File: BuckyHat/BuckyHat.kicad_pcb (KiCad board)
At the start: 6 copper layers, 97.2 x 53.7 mm, 95 parts, among them IC1 LM61495Q4RPHRQ1, IC2 LM61495Q4RPHRQ1, IC3 LM61495Q4RPHRQ1, IC4 LM61495Q4RPHRQ1, J1 XT30AW-M, J2 XT30UPB-F, J3 XT30AW-M, J4 XT30UPB-F, J5 XT30AW-M, J6 XT30UPB-F, J7 XT30AW-M, J8 XT30UPB-F

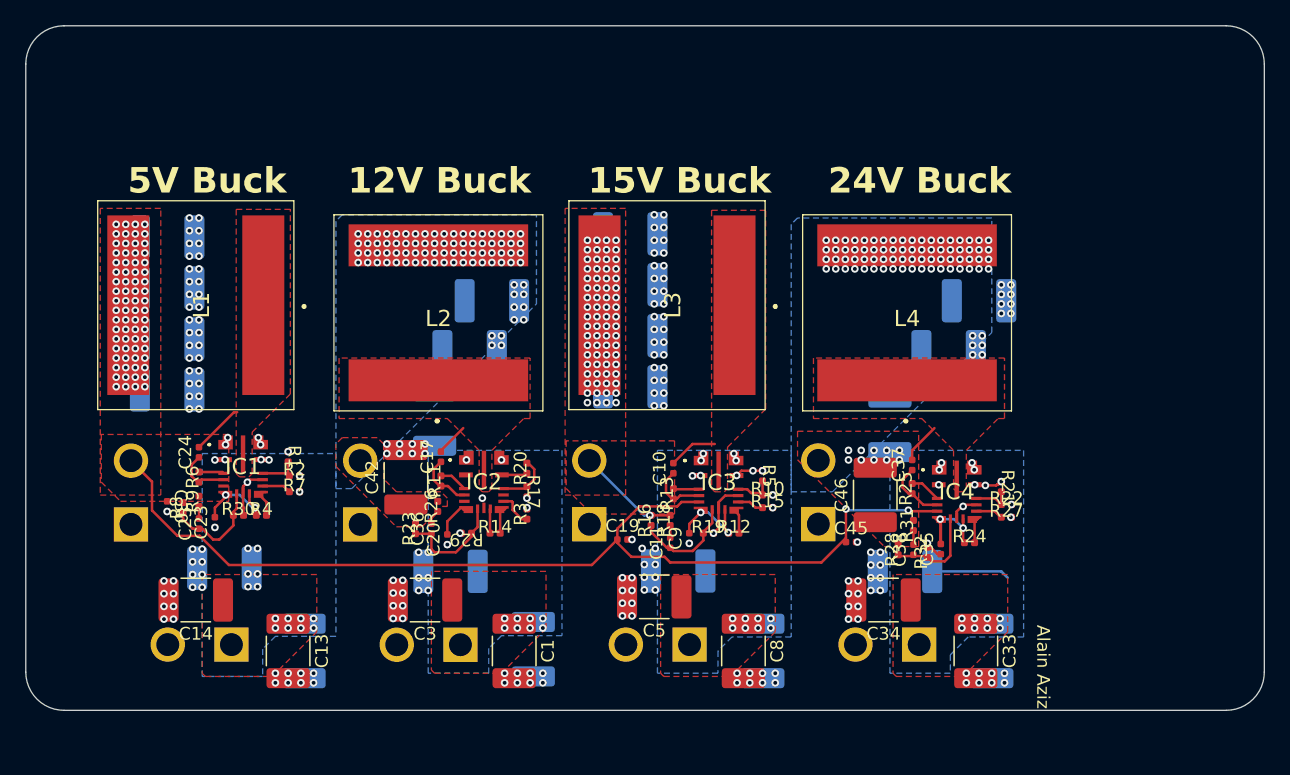
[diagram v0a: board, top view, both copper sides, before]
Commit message: no DRC errors
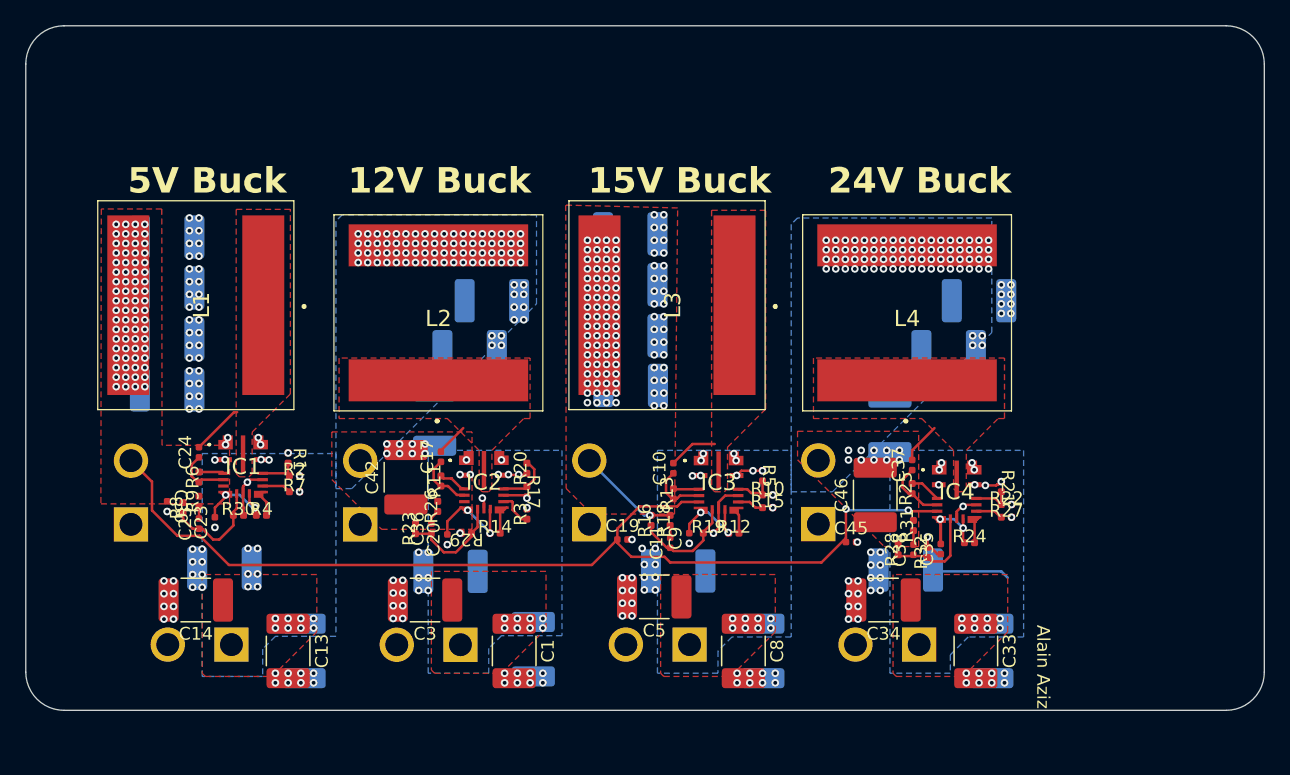
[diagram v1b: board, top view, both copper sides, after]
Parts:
- moved C32 0.13 mm to (217.0, 90.4)
- moved C18 0.11 mm to (195.4, 75.9)
- moved R1 0.10 mm to (168.5, 81.6)
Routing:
- net GND: track 11.9 -> 15.5 mm, vias 236 -> 234
- net Net-(IC2-RT): track 5.13 -> 7.65 mm, vias 0 -> 2
- net /Project Architecture/12VBuck/Vin: vias 8 -> 13
